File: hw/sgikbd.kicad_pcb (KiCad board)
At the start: 2 copper layers, 80 x 60 mm, 32 parts, among them J1 AVR-ISP, SW1 RESET, U1 ATmega328PB, U2 ps2kbd, U3 ps2aux, U4 LM358, U5 sgi-mdin6, U6 L7805, U7 L7905, U8 sgi-db9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

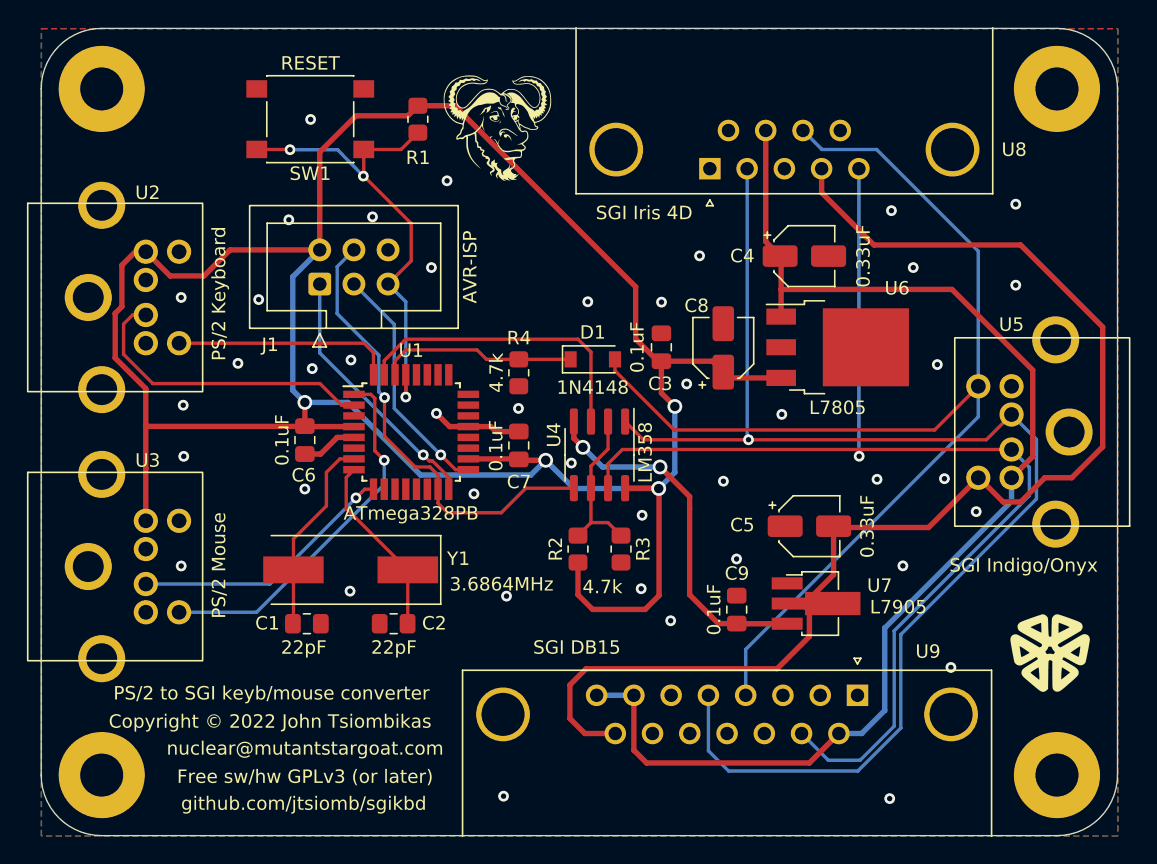
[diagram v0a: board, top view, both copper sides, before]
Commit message: fixed UART polarity
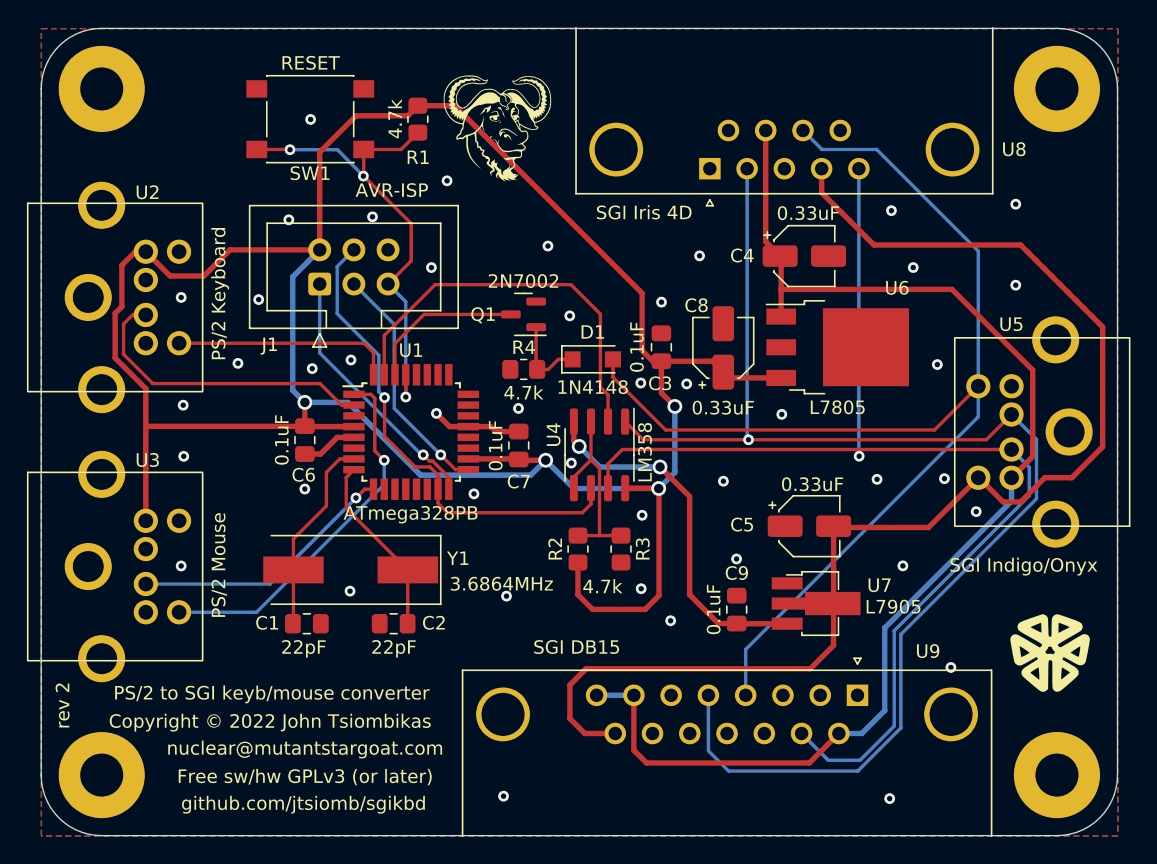
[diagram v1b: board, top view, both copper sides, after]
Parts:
- added Q1: 2N7002, Package_TO_SOT_SMD:SOT-23, F.Cu at (135.8, 81.2)
- moved R4 0.45 mm to (135.8, 85.3), turned to 180 degrees
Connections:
- D1 pad 1: /RXD0 -> Net-(D1-Pad1)
- R4 pad 1: /RXD0 -> Net-(D1-Pad1)
- U4 pad 2: /VREF -> /TXD0
- U4 pad 3: /TXD0 -> /VREF
- U4 pad 5: /TXD1_MOSI -> /VREF
- U4 pad 6: /VREF -> /TXD1_MOSI
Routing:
- net /TXD0: track 22.6 -> 29.7 mm
- net Net-(D1-Pad1): track 0.00 -> 6.12 mm
- net /RXD0: track 14.7 -> 11.8 mm
- net /VREF: track 12.0 -> 14.6 mm
- net /VBUS-: track 96.9 -> 99.1 mm
- net /TXD1_MOSI: track 34.2 -> 36.2 mm
- net GND: vias 42 -> 44
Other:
- board text added: "CLK"
- board text added: "DATA"
- board text added: "GND"
- board text added: "KRX"
- board text added: "KTX"
- board text added: "MRX"
- board text added: "V+"
- board text added: "V-"
- board text added: "VCC"
- board text added: "rev 2"
